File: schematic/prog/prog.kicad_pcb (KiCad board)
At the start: 2 copper layers, 50.8 x 10.2 mm, 26 parts, among them J1 Conn_01x04, J2 Conn_01x01, J3 Conn_01x01, J4 Conn_01x01, J5 Conn_01x01, J6 Conn_01x01, Q1 BC847, Q2 BC847, U1 FT231XS

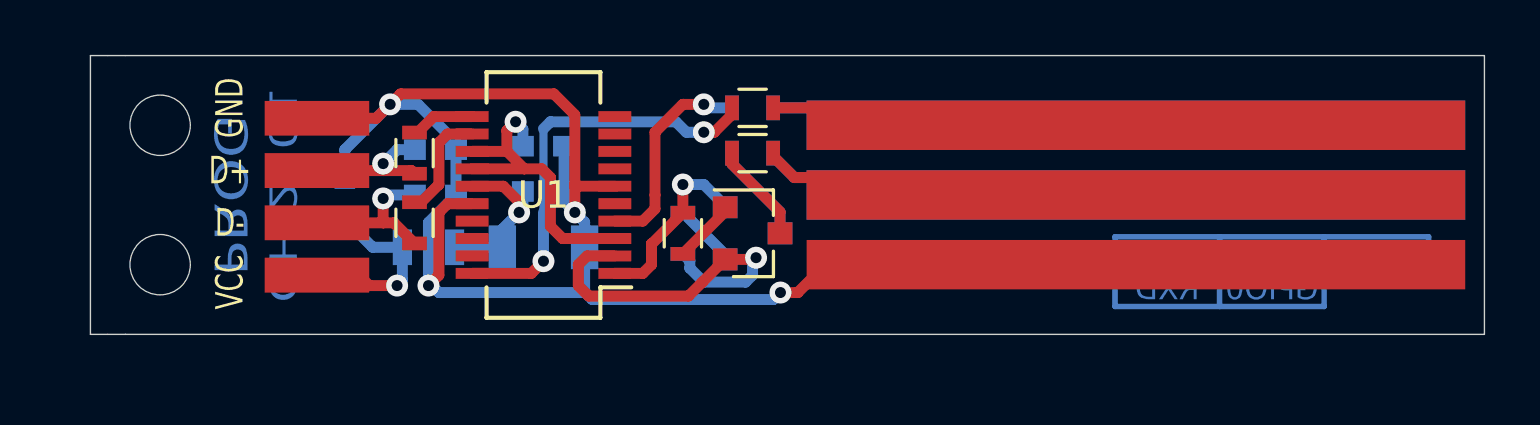
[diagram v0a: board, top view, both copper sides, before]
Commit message: panelizing markers and adjustment
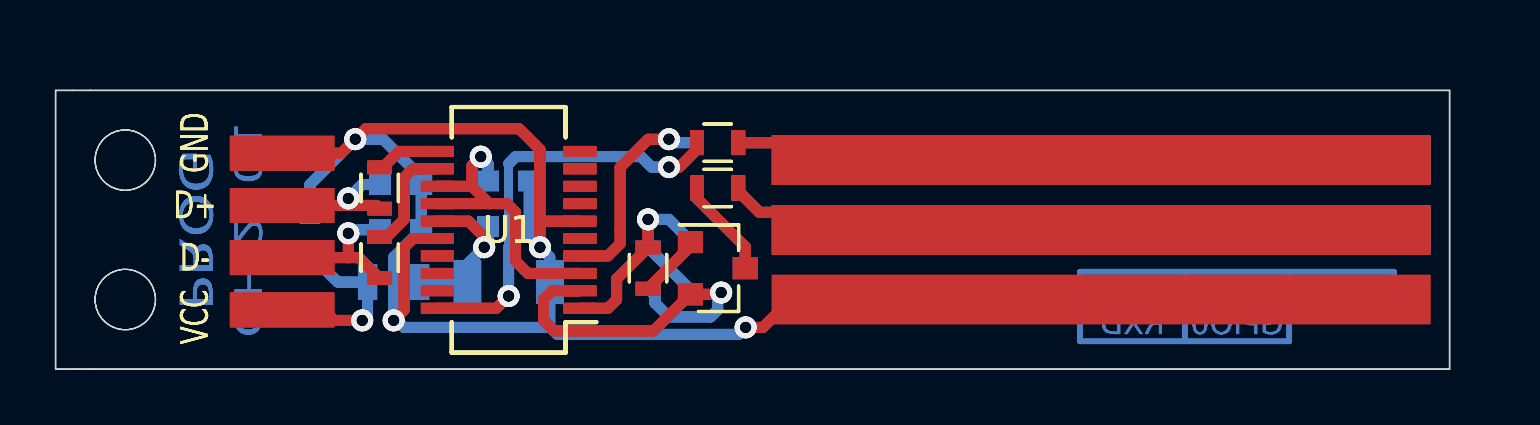
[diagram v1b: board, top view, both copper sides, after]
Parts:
- added C1: 10n, Capacitors_SMD:C_0603, B.Cu at (164.2, 73.8)
- added C2: 47p, Capacitors_SMD:C_0603, B.Cu at (167.5, 73.7)
- added C3: 47p, Capacitors_SMD:C_0603, B.Cu at (167.5, 72.0)
- added C4: 100n, Capacitors_SMD:C_0603, B.Cu at (171.4, 73.5)
- added C5: 4u7, Capacitors_SMD:C_1206, B.Cu at (171.4, 75.6)
- added C6: 100n, Capacitors_SMD:C_0603, B.Cu at (171.4, 71.9)
- added FB1: Ferrite_Bead_Small, Resistors_SMD:R_0805, B.Cu at (167.3, 75.6)
- added H1: MountingHole, Mounting_Holes:MountingHole_2.2mm_M2, F.Cu at (157.5, 71.1)
- added H2: MountingHole, Mounting_Holes:MountingHole_2.2mm_M2, F.Cu at (157.5, 76.2)
- added J1: Conn_01x04, keg01:SOLDER_CONN_4p, F.Cu at (163.2, 73.4)
- added J2: Conn_01x01, keg01:POGO_FLAT, F.Cu at (193.0, 71.1)
- added J3: Conn_01x01, keg01:POGO_FLAT, B.Cu at (193.0, 71.1)
- added J4: Conn_01x01, keg01:POGO_FLAT, F.Cu at (193.0, 73.7)
- added J5: Conn_01x01, keg01:POGO_FLAT, B.Cu at (193.0, 73.7)
- added J6: Conn_01x01, keg01:POGO_FLAT, F.Cu at (193.0, 76.2)
- added Q1: BC847, TO_SOT_Packages_SMD:SOT-23, F.Cu at (179.1, 75.1)
- added Q2: BC847, TO_SOT_Packages_SMD:SOT-23, B.Cu at (179.1, 75.1)
- added R1: 27, Resistors_SMD:R_0603, F.Cu at (166.8, 74.7)
- added R2: 27, Resistors_SMD:R_0603, F.Cu at (166.8, 72.1)
- added R3: 10k, Resistors_SMD:R_0603, F.Cu at (176.5, 75.1)
- added R4: 10k, Resistors_SMD:R_0603, B.Cu at (176.5, 75.1)
- added R5: 100, Resistors_SMD:R_0603, F.Cu at (179.1, 70.5)
- added R6: 100, Resistors_SMD:R_0603, B.Cu at (179.1, 70.5)
- added R7: 100, Resistors_SMD:R_0603, F.Cu at (179.1, 72.1)
- added R8: 100, Resistors_SMD:R_0603, B.Cu at (179.1, 72.1)
- added U1: FT231XS, keg01:SSOP-20_3.9x8.7mm_P0.635mm, F.Cu at (171.4, 73.7)
- moved C6 1.80 mm to (171.4, 71.9)
- moved H1 1.80 mm to (157.5, 71.1)
- moved J1 1.80 mm to (163.2, 73.4)
- moved J2 1.80 mm to (193.0, 71.1)
- moved J3 1.80 mm to (193.0, 71.1)
- moved C4 1.80 mm to (171.4, 73.5)
- moved C5 1.80 mm to (171.4, 75.6)
- moved FB1 1.80 mm to (167.3, 75.6)
- moved H2 1.80 mm to (157.5, 76.2)
- moved J4 1.80 mm to (193.0, 73.7)
- moved J5 1.80 mm to (193.0, 73.7)
- moved J6 1.80 mm to (193.0, 76.2)
- moved Q1 1.80 mm to (179.1, 75.1)
- moved Q2 1.80 mm to (179.1, 75.1)
- moved R3 1.80 mm to (176.5, 75.1)
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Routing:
- net GND: track 63.5 -> 126.9 mm, vias 4 -> 8
- net /TXD: track 15.3 -> 30.5 mm, vias 2 -> 4
- net /_RST: track 13.9 -> 27.8 mm
- net /_GPIO0: track 13.9 -> 27.8 mm
- net /_TXD: track 13.5 -> 27.0 mm
- net /_RXD: track 13.5 -> 27.0 mm
- net /RTS: track 13.4 -> 26.8 mm, vias 1 -> 2
- net Net-(C6-Pad2): track 11.7 -> 23.3 mm, vias 1 -> 2
- net /RXD: track 7.72 -> 15.4 mm, vias 1 -> 2
- net Net-(C1-Pad2): track 7.09 -> 14.2 mm, vias 1 -> 2
- net /DTR: track 6.78 -> 13.6 mm, vias 1 -> 2
- net Net-(C4-Pad2): track 6.41 -> 12.8 mm, vias 1 -> 2
- net Net-(C2-Pad2): track 5.96 -> 11.9 mm, vias 1 -> 2
- net Net-(C3-Pad2): track 5.48 -> 11.0 mm, vias 1 -> 2
- net Net-(R1-Pad1): track 4.02 -> 8.05 mm
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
